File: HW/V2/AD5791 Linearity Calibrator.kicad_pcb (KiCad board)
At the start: 4 copper layers, 80 x 100 mm, 69 parts, among them J2 VREFP, J3 VREFN, J5 VREFP, J6 ISO OUT, J7 PWR, SW1 RST, U1 LM317, U10 ADR1399, U2 LM337, U3 LM317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

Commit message: updated layout
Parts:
- removed D1: 5819, Resistor_SMD:R_0603_1608Metric_Pad0.98x0.95mm_HandSolder
- removed JP2: MECCA, Connector_PinHeader_1.27mm:PinHeader_1x02_P1.27mm_Vertical
- added C17: 10uF, Resistor_SMD:R_0603_1608Metric, F.Cu at (128.2, 66.0)
- added C18: 10uF, Resistor_SMD:R_0603_1608Metric, F.Cu at (111.8, 66.0)
- added C19: 10uF, Resistor_SMD:R_0603_1608Metric, F.Cu at (91.8, 66.0)
- moved C16 1.97 mm to (90.0, 121.2), turned to 180 degrees
- moved R10 0.25 mm to (131.8, 64.5)
- moved R11 0.25 mm to (128.2, 64.5)
- moved R12 0.25 mm to (88.2, 64.5)
- moved R13 0.25 mm to (91.8, 64.5)
- moved R14 0.25 mm to (108.2, 64.5)
- moved R15 0.25 mm to (111.8, 64.5)
- moved R9 0.25 mm to (100.0, 94.2)
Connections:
- C8 pad 2: GNDA -> GND
- J4 pad 2: GNDA -> GND
- J7 pad 1: unconnected-(J7-Pin_1-Pad1) -> +15V
- J7 pad 2: unconnected-(J7-Pin_2-Pad2) -> -15V
- J7 pad 3: unconnected-(J7-Pin_3-Pad3) -> +3.3V
- J7 pad 4: unconnected-(J7-Pin_4-Pad4) -> GND
- U10 pad 2: GNDA -> GND
- U5 pad 11: /SDO -> unconnected-(U5-SDO-Pad11)
- U5 pad 19: GNDA -> GND
- U6 pad 3: GNDA -> GND
- U8 pad 10: /~{RESET} -> /~{LDAC}
- U8 pad 12: /~{LDAC} -> /~{RESET}
- U8 pad 5: /SDO -> unconnected-(U8-GPIO3-Pad5)
- U9 pad 5: GNDA -> GND
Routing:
- net /UART_TX: track 0.00 -> 64.4 mm
- net /UART_RX: track 0.00 -> 63.0 mm
- net GNDA: track 28.3 -> 0.00 mm, vias 3 -> 0
- net /~{SYNC}: track 1.32 -> 25.1 mm, vias 1 -> 0
- net GND: track 13.0 -> 36.5 mm, vias 37 -> 42
- net /ISO_VDD: track 2.45 -> 25.3 mm, vias 0 -> 1
- net /SDIN: track 1.32 -> 22.4 mm, vias 1 -> 0
- net /ISO_TX: track 0.00 -> 20.8 mm, vias 0 -> 1
- net /~{RESET}: track 1.32 -> 21.5 mm
- net /SCLK: track 1.82 -> 21.6 mm, vias 1 -> 0
- net /ISO_RX: track 0.00 -> 18.5 mm, vias 0 -> 1
- net /~{CLR}: track 1.82 -> 20.0 mm
- net /ISO_GND: track 0.92 -> 18.3 mm
- net /~{LDAC}: track 1.32 -> 18.0 mm
- net /7VREF: track 29.4 -> 40.0 mm
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- added copper zone on In2.Cu, net -15V
- added copper zone on B.Cu, net GND
- added copper zone on In1.Cu, net GND
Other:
- board text added: "RESET"
- board text removed: "MECCA"

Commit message: updated files
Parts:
- added U11: ADuM1400xRW, Package_SO:SOIC-16W_7.5x10.3mm_P1.27mm, F.Cu at (135.0, 127.0)
- added U12: ISO7340C, Package_SO:SOIC-16W_7.5x10.3mm_P1.27mm, F.Cu at (179.8, 117.8)
- moved C15 48.3 mm to (49.7, 108.8)
- moved C16 48.3 mm to (47.8, 97.8)
- moved J6 48.3 mm to (31.2, 99.2)
- moved U4 48.3 mm to (47.8, 103.0)
- moved SW1 40.2 mm to (162.5, 132.5)
- moved U8 29.1 mm to (95.5, 128.8), turned to 90 degrees
- moved C13 12.5 mm to (133.6, 94.2), turned to -90 degrees
- moved C9 12.1 mm to (123.4, 105.8), turned to 90 degrees
- moved R5 12.1 mm to (119.6, 94.2), turned to -90 degrees
- moved C10 11.8 mm to (137.4, 105.8), turned to 90 degrees
- moved R6 11.7 mm to (134.9, 94.2), turned to -90 degrees
- moved C12 11.6 mm to (120.9, 94.2), turned to -90 degrees
- moved R2 11.6 mm to (122.1, 105.8), turned to 90 degrees
- moved R3 11.5 mm to (136.1, 105.8), turned to 90 degrees
- moved REF** 3.25 mm to (108.8, 126.8), turned to 90 degrees
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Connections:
- J7 pad 1: +15V -> -15V
- J7 pad 2: -15V -> +15V
- U7 pad 1: /VREFPF -> /VREFNF
- U7 pad 2: /VREFPS -> /VREFNS
- U7 pad 3: /+10.5V -> /-10.5V
- U7 pad 5: /-10.5V -> /+10.5V
- U7 pad 6: /VREFNS -> /VREFPS
- U7 pad 7: /VREFNF -> /VREFPF
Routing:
- net /UART_TX: track 64.4 -> 0.00 mm
- net /UART_RX: track 63.0 -> 0.00 mm
- net GND: track 36.5 -> 84.8 mm, vias 42 -> 43
- net /~{SYNC}: track 25.1 -> 0.00 mm
- net /SDIN: track 22.4 -> 0.00 mm
- net /SCLK: track 21.6 -> 0.00 mm
- net /~{RESET}: track 21.5 -> 0.00 mm, vias 1 -> 0
- net /~{CLR}: track 20.0 -> 0.00 mm, vias 1 -> 0
- net /~{LDAC}: track 18.0 -> 0.00 mm, vias 1 -> 0
- net /-10.5V: track 26.2 -> 11.0 mm
- net /VREFPF: track 12.0 -> 0.00 mm
- net /VREFNF: track 11.6 -> 0.00 mm
- net /BUFIN: track 22.2 -> 11.7 mm
- net /VREFPS: track 9.32 -> 0.00 mm
- net Net-(J4-Pin_3): track 14.4 -> 5.22 mm
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- removed copper zone on In2.Cu, net -15V

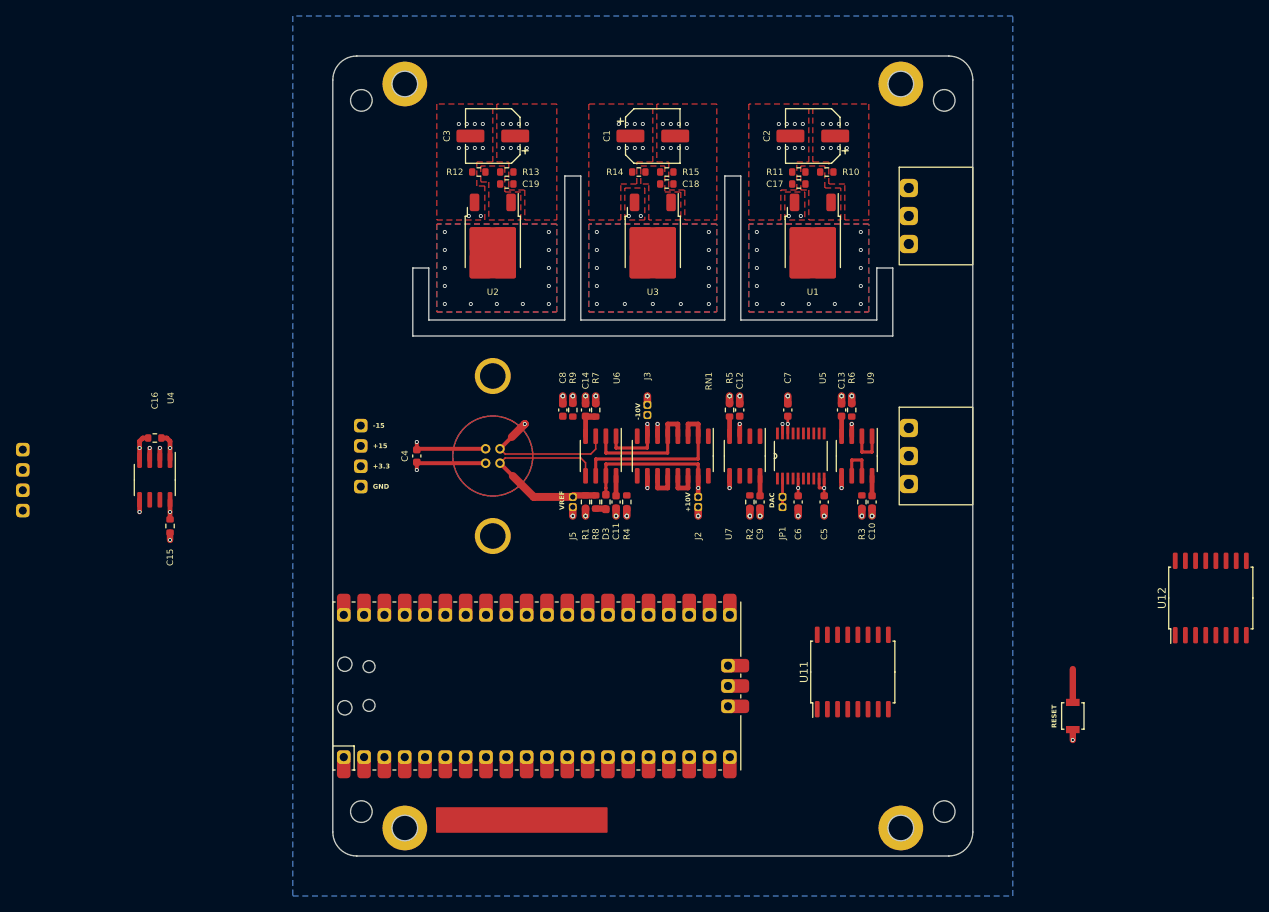
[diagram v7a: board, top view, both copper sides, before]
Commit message: updated layout
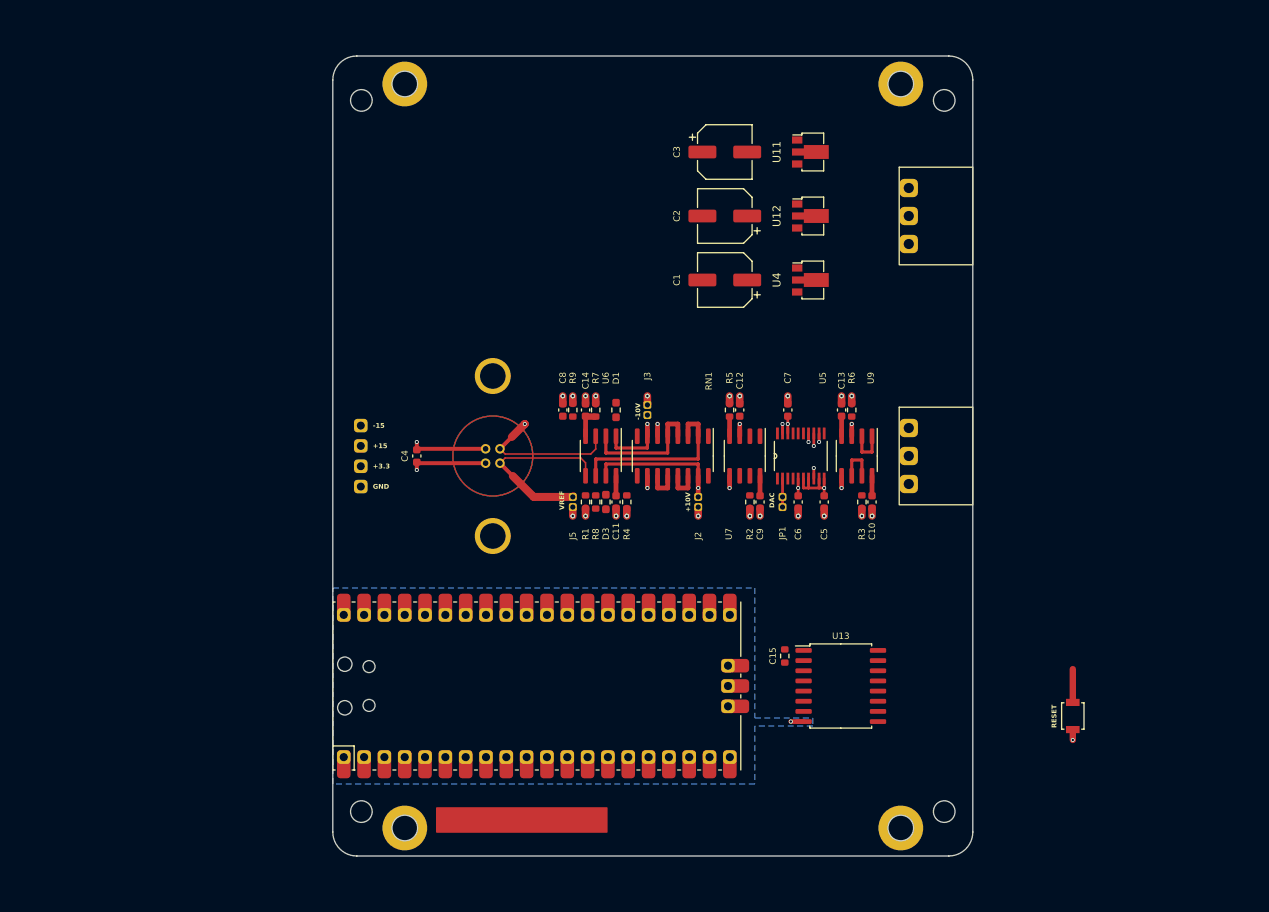
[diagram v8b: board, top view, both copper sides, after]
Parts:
- removed C16, C17, C18, C19: 10uF, Resistor_SMD:R_0603_1608Metric
- removed J6: ISO OUT, Connector_PinHeader_2.54mm:PinHeader_1x04_P2.54mm_Vertical
- removed R10, R12, R14: 220R, Resistor_SMD:R_0603_1608Metric
- removed R11, R13: 2K4, Resistor_SMD:R_0603_1608Metric
- removed R15: 390R, Resistor_SMD:R_0603_1608Metric
- removed U1, U3: LM317, Package_TO_SOT_SMD:TO-252-2
- removed U2: LM337, Package_TO_SOT_SMD:TO-252-2
- added D1: 5819, Resistor_SMD:R_0603_1608Metric_Pad0.98x0.95mm_HandSolder, F.Cu at (105.4, 94.2)
- added U13: ADuM1400xRW, Package_SO:SOIC-16W_7.5x10.3mm_P1.27mm, F.Cu at (133.5, 128.8)
- U11: value ADuM1400xRW -> L79L15; footprint Package_SO:SOIC-16W_7.5x10.3mm_P1.27mm -> Package_TO_SOT_SMD:SOT-89-3
- U12: value ISO7340C -> 7533; footprint Package_SO:SOIC-16W_7.5x10.3mm_P1.27mm -> Package_TO_SOT_SMD:SOT-89-3
- U4: value ADuM1201AR -> L78L15; footprint Package_SO:SOIC-8_3.9x4.9mm_P1.27mm -> Package_TO_SOT_SMD:SOT-89-3
- moved U4 86.0 mm to (130.0, 78.0), turned to 0 degrees
- moved C15 78.5 mm to (126.5, 125.0), turned to 90 degrees
- moved U12 69.0 mm to (130.0, 70.0), turned to 0 degrees
- moved U11 65.2 mm to (130.0, 62.0), turned to 0 degrees
- moved C3 29.1 mm to (119.0, 62.0), turned to 0 degrees
- moved C1 20.1 mm to (119.0, 78.0), turned to 180 degrees
- moved C2 14.9 mm to (119.0, 70.0)
- moved REF** 2.00 mm to (108.8, 128.8)
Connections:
- C15 pad 1: +3.3V -> GNDD
- C15 pad 2: GND -> +3.3VP
- D3 pad 1: Net-(D3-K) -> /+10.5V
- D3 pad 2: /+10.5V -> Net-(D3-A)
- R8 pad 1: /7VREF -> /+10.5V
- R8 pad 2: Net-(D3-K) -> /7VREF
- SW1 pad 1: GND -> GNDD
- U11 pad 1: unconnected-(U11-VDD1-Pad1) -> GND
- U11 pad 2: Net-(U11-GND1-Pad2) -> Net-(J1-Pin_1)
- U11 pad 3: unconnected-(U11-VIA-Pad3) -> -15V
- U12 pad 1: unconnected-(U12-VCC1-Pad1) -> GND
- U12 pad 2: Net-(U12-GND1-Pad2) -> +15V
- U12 pad 3: unconnected-(U12-INA-Pad3) -> +3.3V
- U4 pad 1: /ISO_VDD -> +15V
- U4 pad 2: /ISO_TX -> GND
- U4 pad 3: /ISO_RX -> Net-(J1-Pin_3)
- U5 pad 6: /~{RESET} -> +3.3V
- U5 pad 7: /~{CLR} -> +3.3V
- U6 pad 1: /-10.5V -> Net-(D1-K)
- U6 pad 7: /+10.5V -> Net-(D3-A)
- U8 pad 1: /UART_TX -> unconnected-(U8-GPIO0-Pad1)
- U8 pad 10: /~{LDAC} -> unconnected-(U8-GPIO7-Pad10)
- U8 pad 11: /~{CLR} -> unconnected-(U8-GPIO8-Pad11)
- U8 pad 12: /~{RESET} -> unconnected-(U8-GPIO9-Pad12)
- U8 pad 13: GND -> GNDD
- U8 pad 18: GND -> GNDD
- U8 pad 2: /UART_RX -> unconnected-(U8-GPIO1-Pad2)
- U8 pad 23: GND -> GNDD
- U8 pad 28: GND -> GNDD
- U8 pad 3: GND -> GNDD
- U8 pad 33: GND -> GNDD
- U8 pad 36: +3.3V -> +3.3VP
- U8 pad 37: GND -> unconnected-(U8-3V3_EN-Pad37)
- U8 pad 38: GND -> GNDD
- U8 pad 42: GND -> GNDD
- U8 pad 6: /SDIN -> unconnected-(U8-GPIO4-Pad6)
- U8 pad 7: /SCLK -> unconnected-(U8-GPIO5-Pad7)
- U8 pad 8: GND -> GNDD
- U8 pad 9: /~{SYNC} -> unconnected-(U8-GPIO6-Pad9)
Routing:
- net /ISO_VDD: track 25.3 -> 0.00 mm, vias 1 -> 0
- net /ISO_TX: track 20.8 -> 0.00 mm, vias 1 -> 0
- net /ISO_RX: track 18.5 -> 0.00 mm, vias 1 -> 0
- net /ISO_GND: track 18.3 -> 0.00 mm, vias 1 -> 0
- net GND: track 84.8 -> 81.0 mm, vias 43 -> 16
- net GNDD: track 0.00 -> 2.90 mm, vias 0 -> 2
- net /7VREF: track 40.0 -> 37.3 mm
- net /+10.5V: track 21.0 -> 18.8 mm
- net +3.3V: track 8.58 -> 10.4 mm, vias 23 -> 1
- net /SCLK: track 0.00 -> 1.57 mm, vias 0 -> 1
- net Net-(D3-K): track 1.54 -> 0.00 mm
- net /~{LDAC}: track 0.00 -> 1.32 mm, vias 0 -> 1
- net /~{SYNC}: track 0.00 -> 1.07 mm, vias 0 -> 1
- net /SDIN: track 0.00 -> 1.07 mm, vias 0 -> 1
- net Net-(J1-Pin_3): vias 2 -> 0
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- added copper zone on B.Cu, net GNDD
- added copper zone on In1.Cu, net GNDD
- added copper zone on In2.Cu, net GNDD
- removed copper zone on B.Cu, net +15V
- removed copper zone on F.Cu, net +15V
- removed copper zone on In1.Cu, net +15V
- removed copper zone on In2.Cu, net +15V
- removed copper zone on B.Cu, net +3.3V
- removed copper zone on F.Cu, net +3.3V
- removed copper zone on In1.Cu, net +3.3V
- removed copper zone on In2.Cu, net +3.3V
- removed copper zone on F.Cu, net -15V
- removed copper zone on B.Cu, net GND
- removed copper zone on F.Cu, net GND
- removed copper zone on In1.Cu, net GND
- removed copper zone on B.Cu, net Net-(J1-Pin_1)
- removed copper zone on F.Cu, net Net-(J1-Pin_1)
- removed copper zone on In1.Cu, net Net-(J1-Pin_1)
- removed copper zone on In2.Cu, net Net-(J1-Pin_1)
- removed copper zone on F.Cu, net Net-(J1-Pin_3)
- removed copper zone on In2.Cu, net Net-(J1-Pin_3)
- removed copper zone on F.Cu, net Net-(U1-ADJ)
- removed copper zone on F.Cu, net Net-(U2-ADJ)
- removed copper zone on F.Cu, net Net-(U3-ADJ)
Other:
- outline, holes or cut-outs redrawn
